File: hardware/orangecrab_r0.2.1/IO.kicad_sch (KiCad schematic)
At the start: 37 parts, among them J3 USB_C_Receptacle_USB2.0, SW1 SW_Push, U9 74HC4067BQ

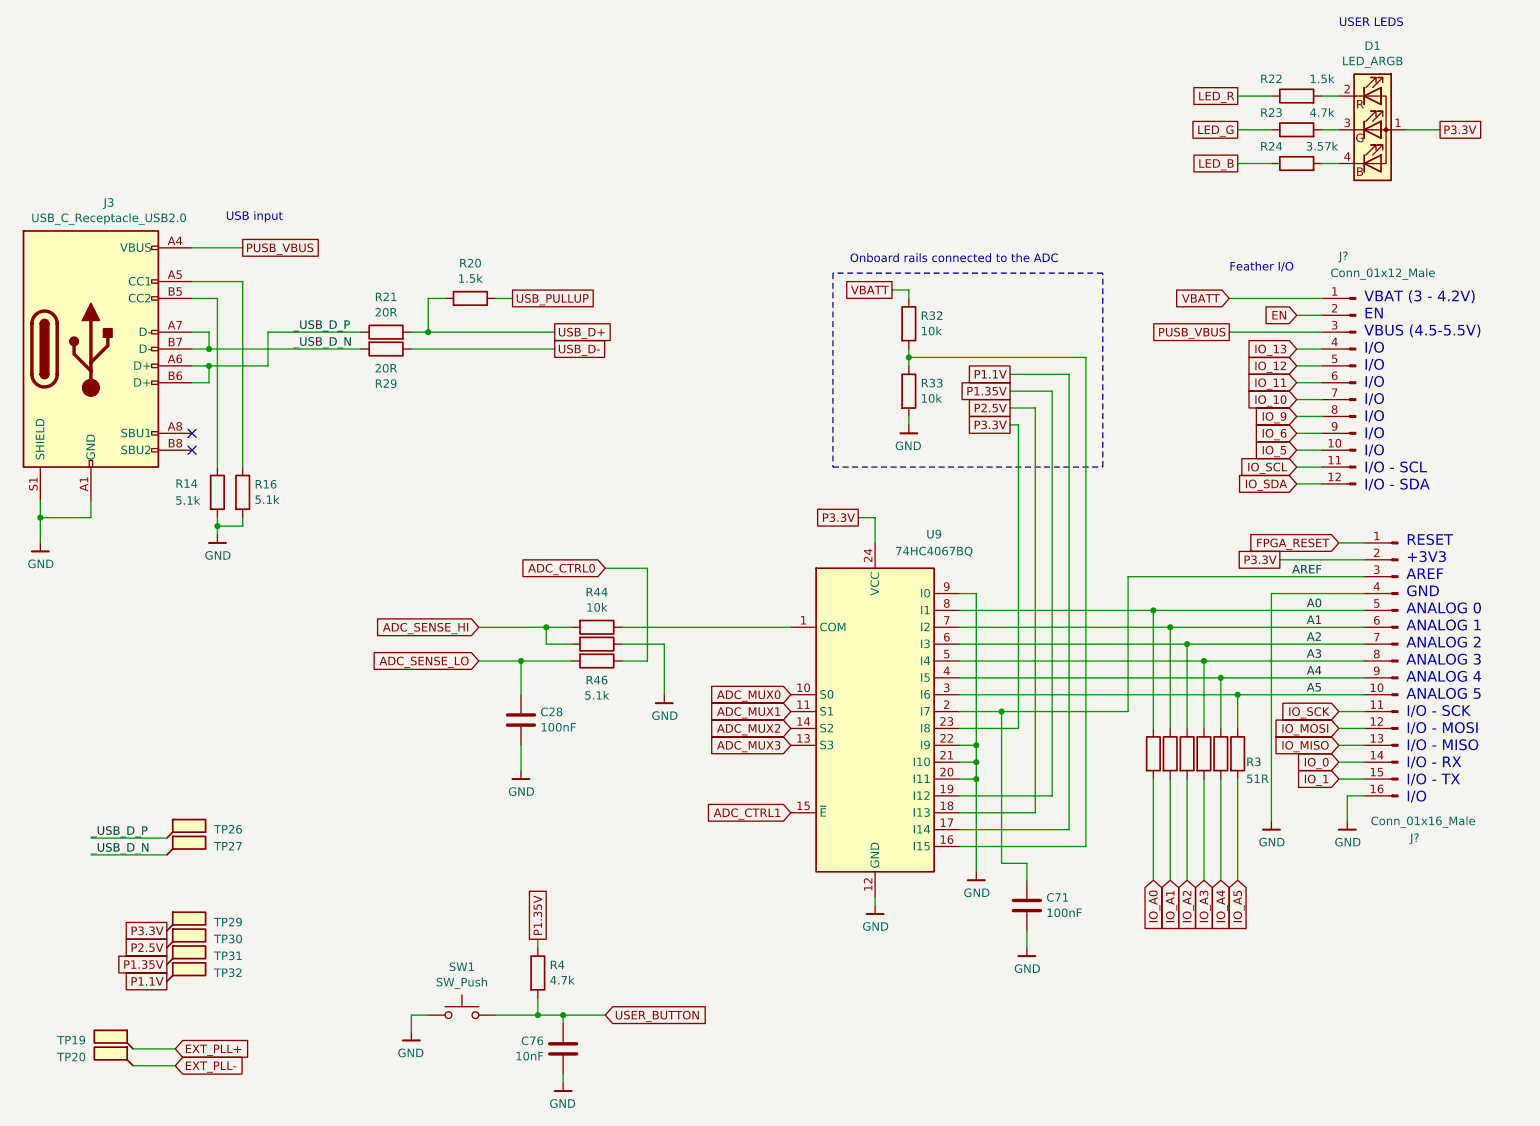
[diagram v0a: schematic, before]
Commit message: Replaced from ECP5U-25 to ECP5UM-25 pinout and added SerDes banks
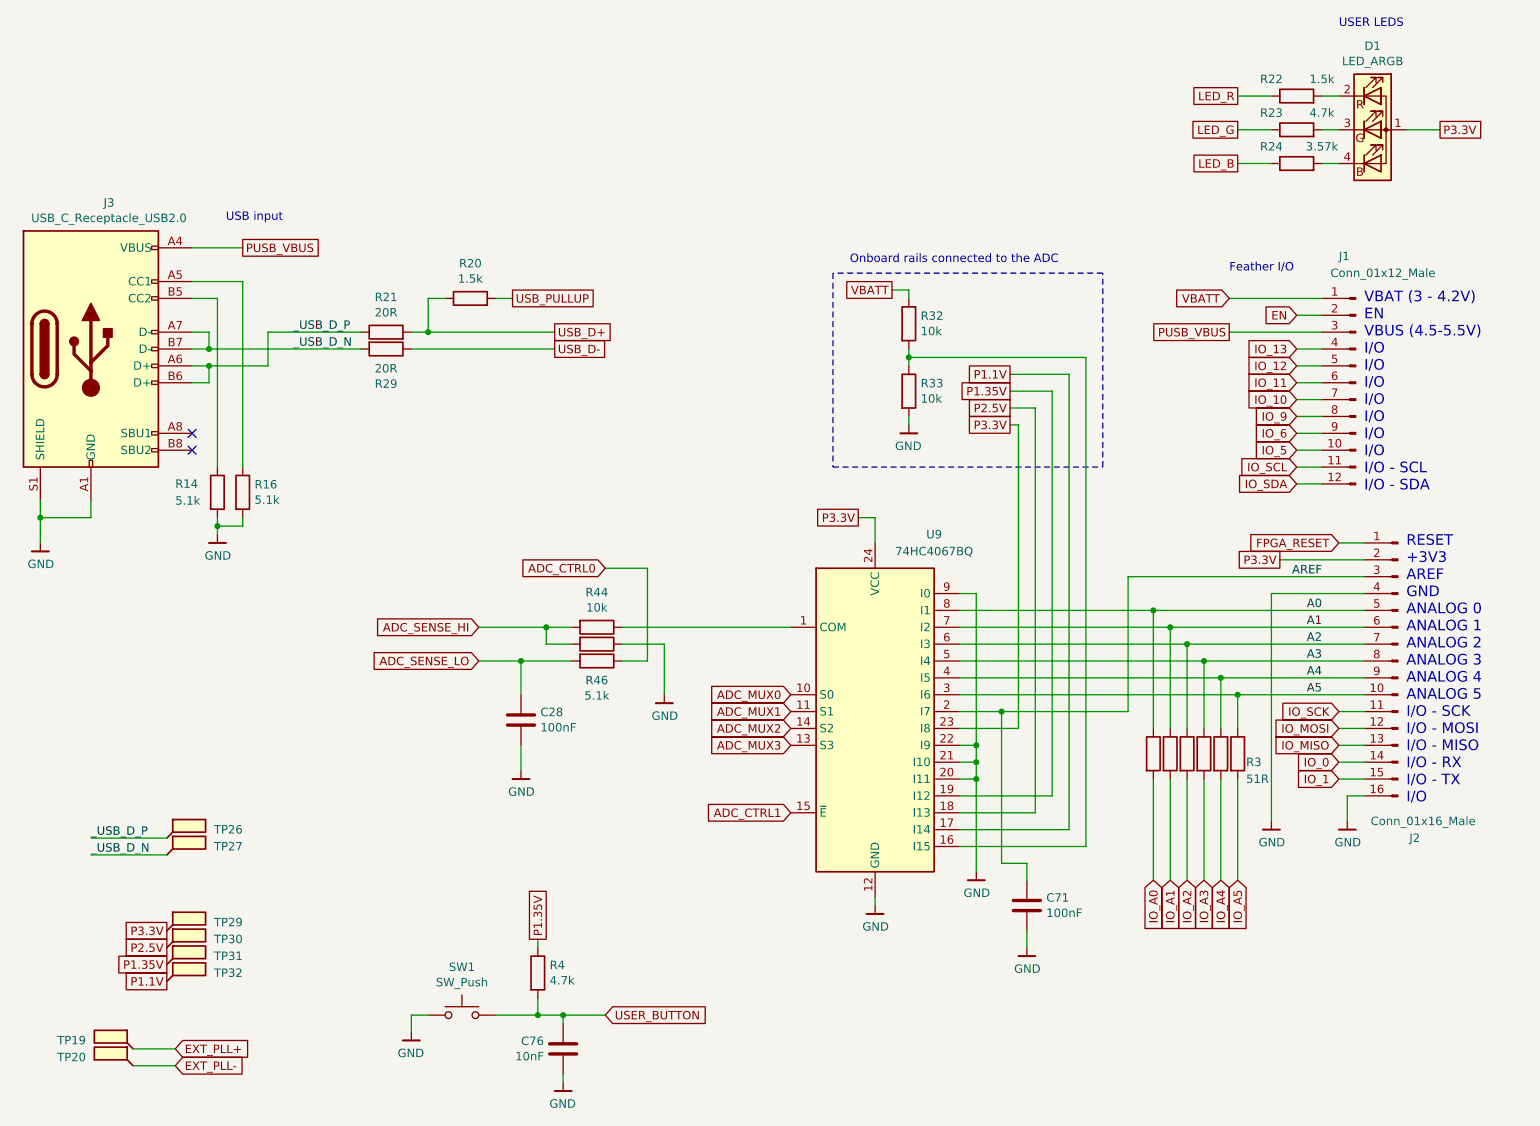
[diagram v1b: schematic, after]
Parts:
- U9: footprint Package_DFN_QFN:Texas_RGY_R-PVQFN-N24_EP2.05x3.1mm -> Package_SO:SOIC-24W_7.5x15.4mm_P1.27mm
- gave numbers to parts that had none: 2
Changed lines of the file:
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@@
     (effects (font (size 1.27 1.27)) (justify left bottom))
   )
-  (label "AREF" (at 218.44 101.6 180)
+  (label "AREF" (at 218.44 101.6 180) (fields_autoplaced)
     (effects (font (size 1.27 1.27)) (justify right bottom))
   )
-  (label "A3" (at 218.44 114.3 180)
+  (label "A3" (at 218.44 114.3 180) (fields_autoplaced)
     (effects (font (size 1.27 1.27)) (justify right bottom))
   )
-  (label "A0" (at 218.44 106.68 180)
+  (label "A0" (at 218.44 106.68 180) (fields_autoplaced)
     (effects (font (size 1.27 1.27)) (justify right bottom))
   )
-  (label "A4" (at 218.44 116.84 180)
+  (label "A4" (at 218.44 116.84 180) (fields_autoplaced)
     (effects (font (size 1.27 1.27)) (justify right bottom))
   )
-  (label "_USB_D_P" (at 63.5 64.77 0)
+  (label "_USB_D_P" (at 63.5 64.77 0) (fields_autoplaced)
     (effects (font (size 1.27 1.27)) (justify left bottom))
   )
-  (label "_USB_D_P" (at 33.02 140.97 0)
+  (label "_USB_D_P" (at 33.02 140.97 0) (fields_autoplaced)
     (effects (font (size 1.27 1.27)) (justify left bottom))
   )
-  (label "_USB_D_N" (at 63.5 67.31 0)
+  (label "_USB_D_N" (at 63.5 67.31 0) (fields_autoplaced)
     (effects (font (size 1.27 1.27)) (justify left bottom))
   )
-  (label "A5" (at 218.44 119.38 180)
+  (label "A5" (at 218.44 119.38 180) (fields_autoplaced)
     (effects (font (size 1.27 1.27)) (justify right bottom))
   )
-  (label "_USB_D_N" (at 33.02 143.51 0)
+  (label "_USB_D_N" (at 33.02 143.51 0) (fields_autoplaced)
     (effects (font (size 1.27 1.27)) (justify left bottom))
   )
-  (label "A2" (at 218.44 111.76 180)
+  (label "A2" (at 218.44 111.76 180) (fields_autoplaced)
     (effects (font (size 1.27 1.27)) (justify right bottom))
   )
-  (label "A1" (at 218.44 109.22 180)
+  (label "A1" (at 218.44 109.22 180) (fields_autoplaced)
     (effects (font (size 1.27 1.27)) (justify right bottom))
   )
@@
   (symbol (lib_id "Connector:Conn_01x16_Male") (at 229.87 114.3 0) (mirror y) (unit 1)
     (in_bom yes) (on_board yes) (dnp no)
-    (property "Reference" "J?" (at 232.41 140.97 0)
+    (property "Reference" "J2" (at 232.41 140.97 0)
       (effects (font (size 1.27 1.27)))
     )
@@
     (instances
       (project "OrangeCrab"
-        (path "/a8599e39-5ed9-4c4e-bc6d-5278922ba9b6/00000000-0000-0000-0000-00005d1738db"
-          (reference "J?") (unit 1)
-        )
         (path "/a8599e39-5ed9-4c4e-bc6d-5278922ba9b6/00000000-0000-0000-0000-00005abc9a87"
           (reference "J2") (unit 1)
@@
   (symbol (lib_id "Connector:Conn_01x12_Male") (at 223.52 72.39 0) (mirror y) (unit 1)
     (in_bom yes) (on_board yes) (dnp no)
-    (property "Reference" "J?" (at 220.98 53.34 0)
+    (property "Reference" "J1" (at 220.98 53.34 0)
       (effects (font (size 1.27 1.27)) (justify right))
     )
@@
     (instances
       (project "OrangeCrab"
-        (path "/a8599e39-5ed9-4c4e-bc6d-5278922ba9b6/00000000-0000-0000-0000-00005d1738db"
-          (reference "J?") (unit 1)
-        )
         (path "/a8599e39-5ed9-4c4e-bc6d-5278922ba9b6/00000000-0000-0000-0000-00005abc9a87"
           (reference "J1") (unit 1)
@@
     )
     (pin "1")
+    (instances
+      (project "OrangeCrab"
+        (path "/a8599e39-5ed9-4c4e-bc6d-5278922ba9b6/00000000-0000-0000-0000-00005abc9a87"
+          (reference "#PWR0133") (unit 1)
+        )
+      )
+    )
   )
   (symbol (lib_id "Connector:TestPoint_Flag") (at 44.45 140.97 0) (unit 1)
@@
           (reference "#PWR0121") (unit 1)
         )
-        (path "/a8599e39-5ed9-4c4e-bc6d-5278922ba9b6/00000000-0000-0000-0000-00005d1738db"
-          (reference "#PWR?") (unit 1)
-        )
       )
     )
@@
     )
     (pin "1")
+    (instances
+      (project "OrangeCrab"
+        (path "/a8599e39-5ed9-4c4e-bc6d-5278922ba9b6/00000000-0000-0000-0000-00005abc9a87"
+          (reference "#PWR0134") (unit 1)
+        )
+      )
+    )
   )
   (symbol (lib_id "Device:LED_ARGB") (at 226.06 34.29 0) (unit 1)
@@
     )
     (pin "1")
+    (instances
+      (project "OrangeCrab"
+        (path "/a8599e39-5ed9-4c4e-bc6d-5278922ba9b6/00000000-0000-0000-0000-00005abc9a87"
+          (reference "#PWR0164") (unit 1)
+        )
+      )
+    )
   )
   (symbol (lib_id "Device:C") (at 104.14 172.72 0) (unit 1)
@@
     )
     (pin "1")
+    (instances
+      (project "OrangeCrab"
+        (path "/a8599e39-5ed9-4c4e-bc6d-5278922ba9b6/00000000-0000-0000-0000-00005abc9a87"
+          (reference "#PWR0165") (unit 1)
+        )
+      )
+    )
   )
   (symbol (lib_id "Device:R") (at 77.47 64.77 90) (unit 1)
@@
       (effects (font (size 1.27 1.27)))
     )
-    (property "Footprint" "Package_DFN_QFN:Texas_RGY_R-PVQFN-N24_EP2.05x3.1mm" (at 173.99 147.32 0)
+    (property "Footprint" "Package_SO:SOIC-24W_7.5x15.4mm_P1.27mm" (at 173.99 147.32 0)
       (effects (font (size 1.27 1.27) italic) hide)
     )
@@
     )
     (pin "1")
+    (instances
+      (project "OrangeCrab"
+        (path "/a8599e39-5ed9-4c4e-bc6d-5278922ba9b6/00000000-0000-0000-0000-00005abc9a87"
+          (reference "#PWR0103") (unit 1)
+        )
+      )
+    )
   )
   (symbol (lib_id "gkl_power:GND") (at 151.13 151.13 0) (unit 1)
@@
     )
     (pin "1")
+    (instances
+      (project "OrangeCrab"
+        (path "/a8599e39-5ed9-4c4e-bc6d-5278922ba9b6/00000000-0000-0000-0000-00005abc9a87"
+          (reference "#PWR0131") (unit 1)
+        )
+      )
+    )
   )
   (symbol (lib_id "Device:C") (at 97.79 123.19 0) (unit 1)
@@
     )
     (pin "1")
+    (instances
+      (project "OrangeCrab"
+        (path "/a8599e39-5ed9-4c4e-bc6d-5278922ba9b6/00000000-0000-0000-0000-00005abc9a87"
+          (reference "#PWR0132") (unit 1)
+        )
+      )
+    )
   )
   (symbol (lib_id "gkl_power:GND") (at 97.79 130.81 0) (unit 1)
@@
     )
     (pin "1")
+    (instances
+      (project "OrangeCrab"
+        (path "/a8599e39-5ed9-4c4e-bc6d-5278922ba9b6/00000000-0000-0000-0000-00005abc9a87"
+          (reference "#PWR0160") (unit 1)
+        )
+      )
+    )
   )
   (symbol (lib_id "Device:C") (at 173.99 151.13 0) (unit 1)
@@
     )
     (pin "1")
+    (instances
+      (project "OrangeCrab"
+        (path "/a8599e39-5ed9-4c4e-bc6d-5278922ba9b6/00000000-0000-0000-0000-00005abc9a87"
+          (reference "#PWR0161") (unit 1)
+        )
+      )
+    )
   )
   (symbol (lib_id "Device:R") (at 156.21 73.66 0) (unit 1)
@@
     )
     (pin "1")
+    (instances
+      (project "OrangeCrab"
+        (path "/a8599e39-5ed9-4c4e-bc6d-5278922ba9b6/00000000-0000-0000-0000-00005abc9a87"
+          (reference "#PWR0172") (unit 1)
+        )
+      )
+    )
   )
   (symbol (lib_id "Device:R") (at 203.2 128.27 0) (unit 1)
@@
           (reference "#PWR0109") (unit 1)
         )
-        (path "/a8599e39-5ed9-4c4e-bc6d-5278922ba9b6/00000000-0000-0000-0000-00005d1738db"
-          (reference "#PWR?") (unit 1)
-        )
-      )
+      )
